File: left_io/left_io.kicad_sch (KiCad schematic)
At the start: 0 parts

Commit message: Board split Phase 2.4: trim center board, FPC boundary contracts, per-project verification
Center (ducktop2) loses the four sheets that moved to the daughterboards:
04_usb_c_io, 05_power_inputs, 06_tcp0_external_hdmi, 16_gigabit_ethernet,
and the pack-protection section of 01_power_battery (BMS board). J190 AUX
terminal moves to the left board. Center keeps 9 sheets: charger/gauge/
ship-FET (U2/U10/Q25/RS1), EC, Mu, radio, internal, radio-DB, keyboard x2,
maker, audio. 717 components.

FPC-1/2/3 boundary contracts declare the crossing nets at the center root
(30 + 35 + 4 shared nets; HUB_DS1_DP/DM are center pass-throughs).

Verification is now per-project:
- verify_design_contracts.py --project {ducktop2,left_io,right_io,bms}
  (five-port USB-C contracts split by port, HDMI/GbE run on right_io,
  pack contracts run on bms, sheet names parameterized)
- verify_schematic_closure.py --pack audits the BMS pack block
- verify_electrical_calculations.py --project bms for pack calcs
- pin review trimmed to center parts; FPC-boundary nets in ERC allowlist

Fixed while trimming: daughterboard root labels now sit on sheet-block pin
endpoints (left/right FPC nets actually connect); duplicate GND pwrflag in
power sheet; sync.parse_netlist respects the radio-daughterboard override.

Schematic gate PASS: self-check, closure audits (89+151), electrical
calcs (67+15), pin review (1625), identity.
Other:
- sheet PD1 Dual-Role ports: added none; removed HUB_DS1_DM, HUB_DS1_DP, INTERNAL_USB_VBUS_VALID, USBC2_DM, USBC2_DP, USBC2_SSRX_N, USBC2_SSRX_P, USBC2_SSTX_N, USBC2_SSTX_P, VSYS
- sheet USB Hub + Ports ports: added none; removed AUX_DC_RAW, MCU_3V3, PD1_EFUSE_FAULT_N, PD1_I2C_SCL, PD1_I2C_SDA, PD1_PATH_EN, PD1_TCPC_IRQ_N, PD1_VALID_N, PD1_VBUS_RAW, PD2_VALID_N, PD_PROTECT_FAULT_N, USBC1_DM, USBC1_DP, USBC1_SSRX_N, USBC1_SSRX_P, USBC1_SSTX_N, USBC1_SSTX_P, USB_PD_SELECTED

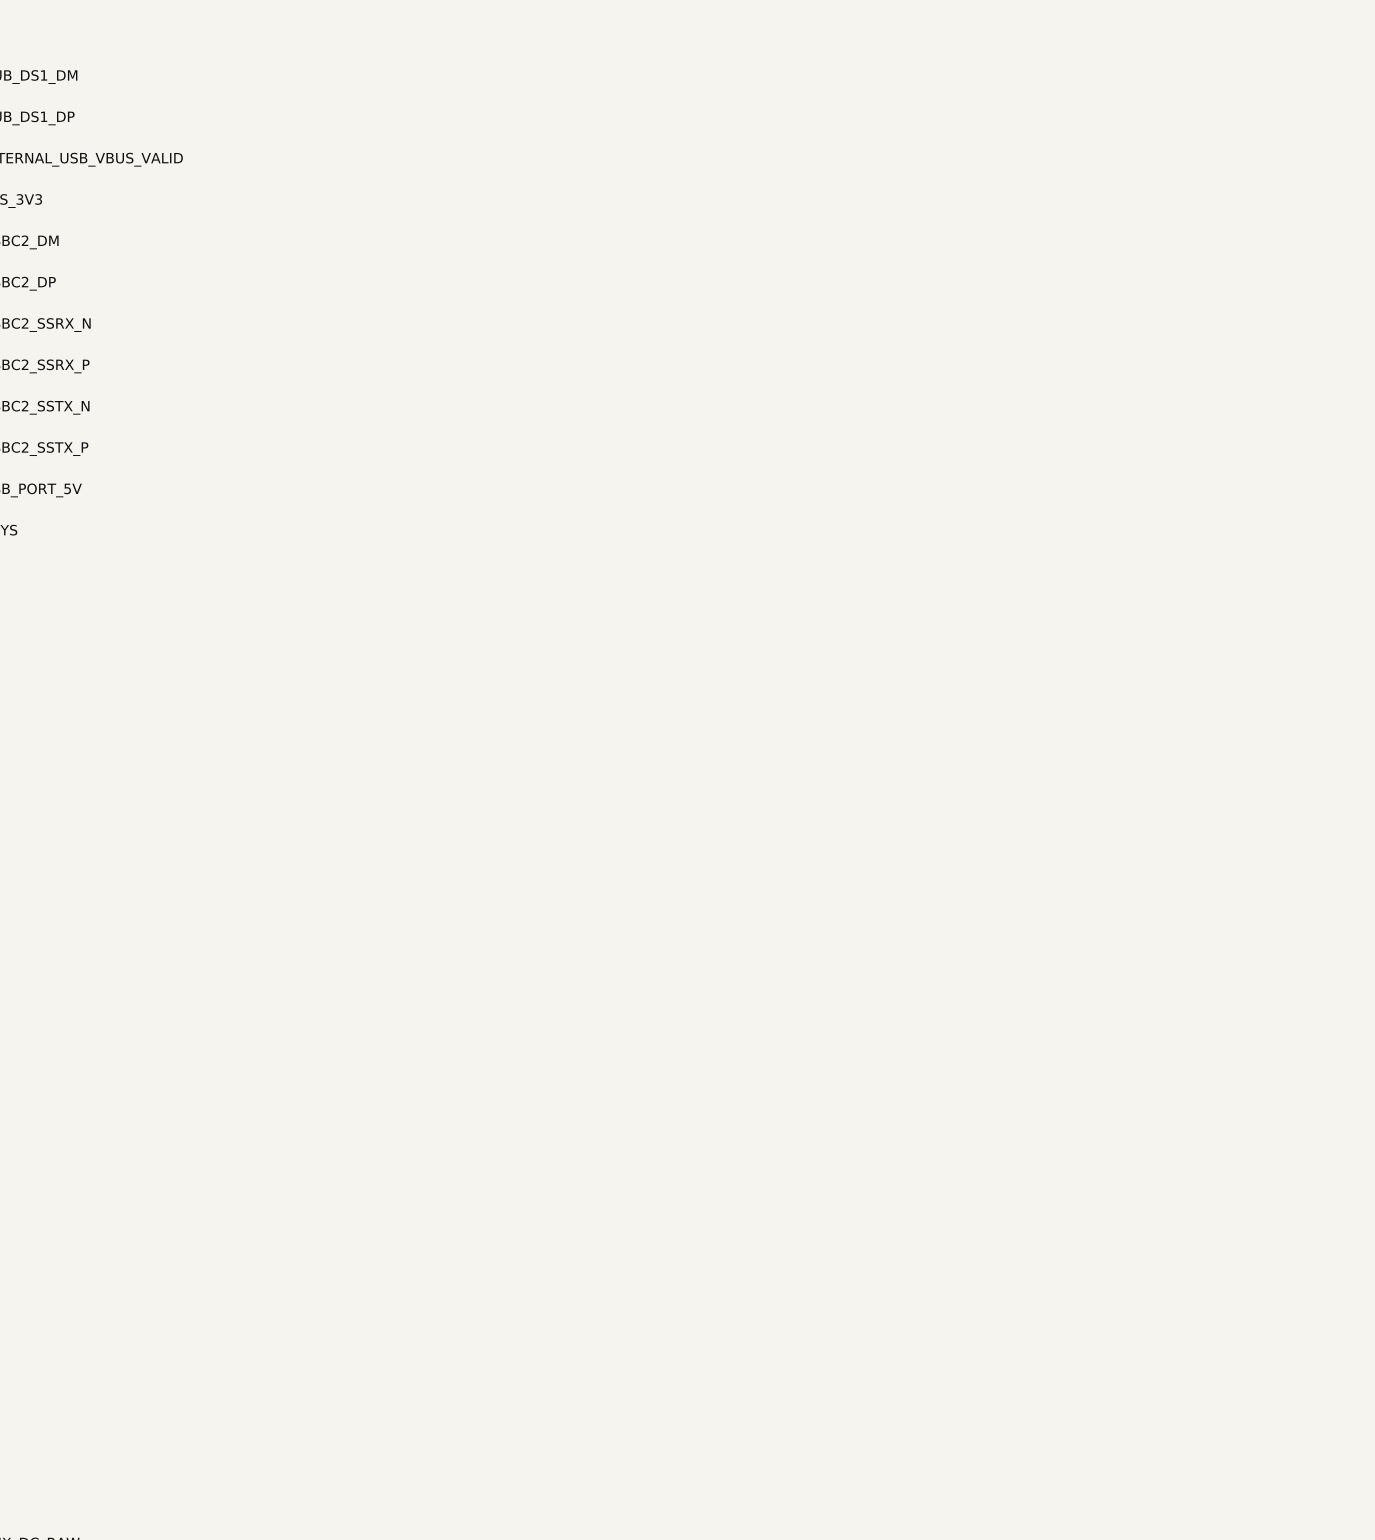
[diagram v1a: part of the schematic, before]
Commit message: Board split Phase 4a: FPC connectors wired through the four split schematics
Connector symbols and sheets now exist in every project and the boundary
nets are pinned through them (same conductor order on both ends, verified
netlist-by-netlist):
  - gen/fpc_contract.py: authoritative FPC-1/2/3 pin maps + center-side
    renames (single source of truth for schematics, board pad nets, cable
    spec, and gate contracts)
  - gen/Conn_01x100_FFC_MP.kicad_sym (derived from the 30-pin pattern)
  - center: real fpc1_left/fpc2_right/fpc3_bms sheets wired to host pins
  - left_io/right_io: left_fpc/right_fpc connector sheets; bms carries
    FPC106 inline
  - connector refs FPC101..FPC106 (valid designators; FPC1_L-style refs
    broke KiCad annotation)
  - pack-rail naming reconciled: center gauge divider BAT_PROT_VIN ->
    PACK_POS_FUSED (same node as the BMS LTC4368 output); BMS ground
    /GND -> GND (pack negative is the system ground)

Boards: daughterboards re-synced from their connector-bearing schematics;
center connectors placed and their pad nets assigned text-side ((net
"name") convention).  Connector pads verified against every other
footprint (0 overlaps) and DRC shows 0 shorts on all four boards (center
16 pre-existing, down from 17).

Fixed two latent generator bugs exposed by the wiring:
  - resolve_connectors used naive +R rotation, placing Phase 3 connectors
    against mirrored phantom positions
  - pad half-extents were computed as footprint_rot+pad_rot, but KiCad
    saves pads with world orientation (FH12-100S pins are 1.3mm wide);
    both verified empirically against pcbnew, plus a connector-nudge pass
    for parts sandwiched between the connector body and pin columns

Gate: SCHEMATIC RELEASE CHECK: PASS (FPC pin contracts added per project;
closure audits 0 FAIL).  Routing remains manual (Phase 4b).
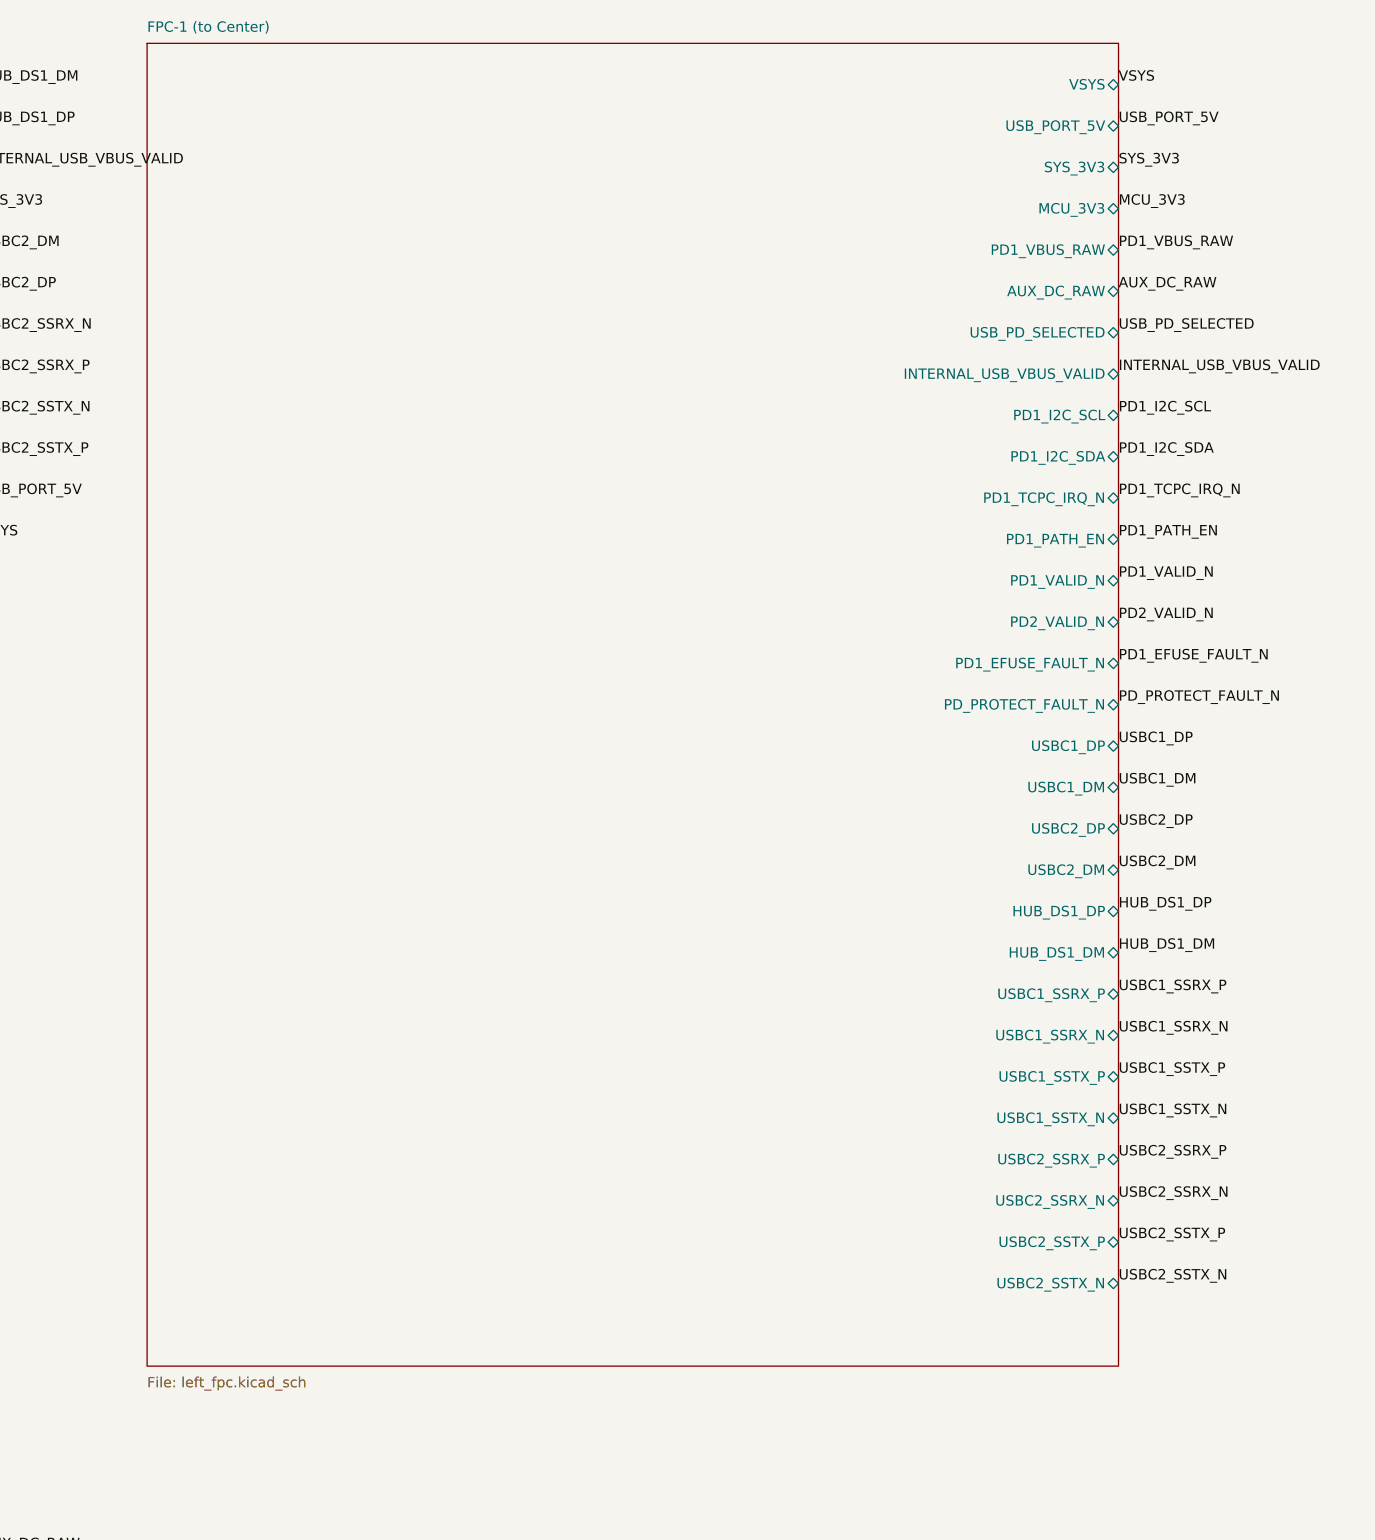
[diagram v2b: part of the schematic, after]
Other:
- added sheet FPC-1 (to Center) (left_fpc.kicad_sch)

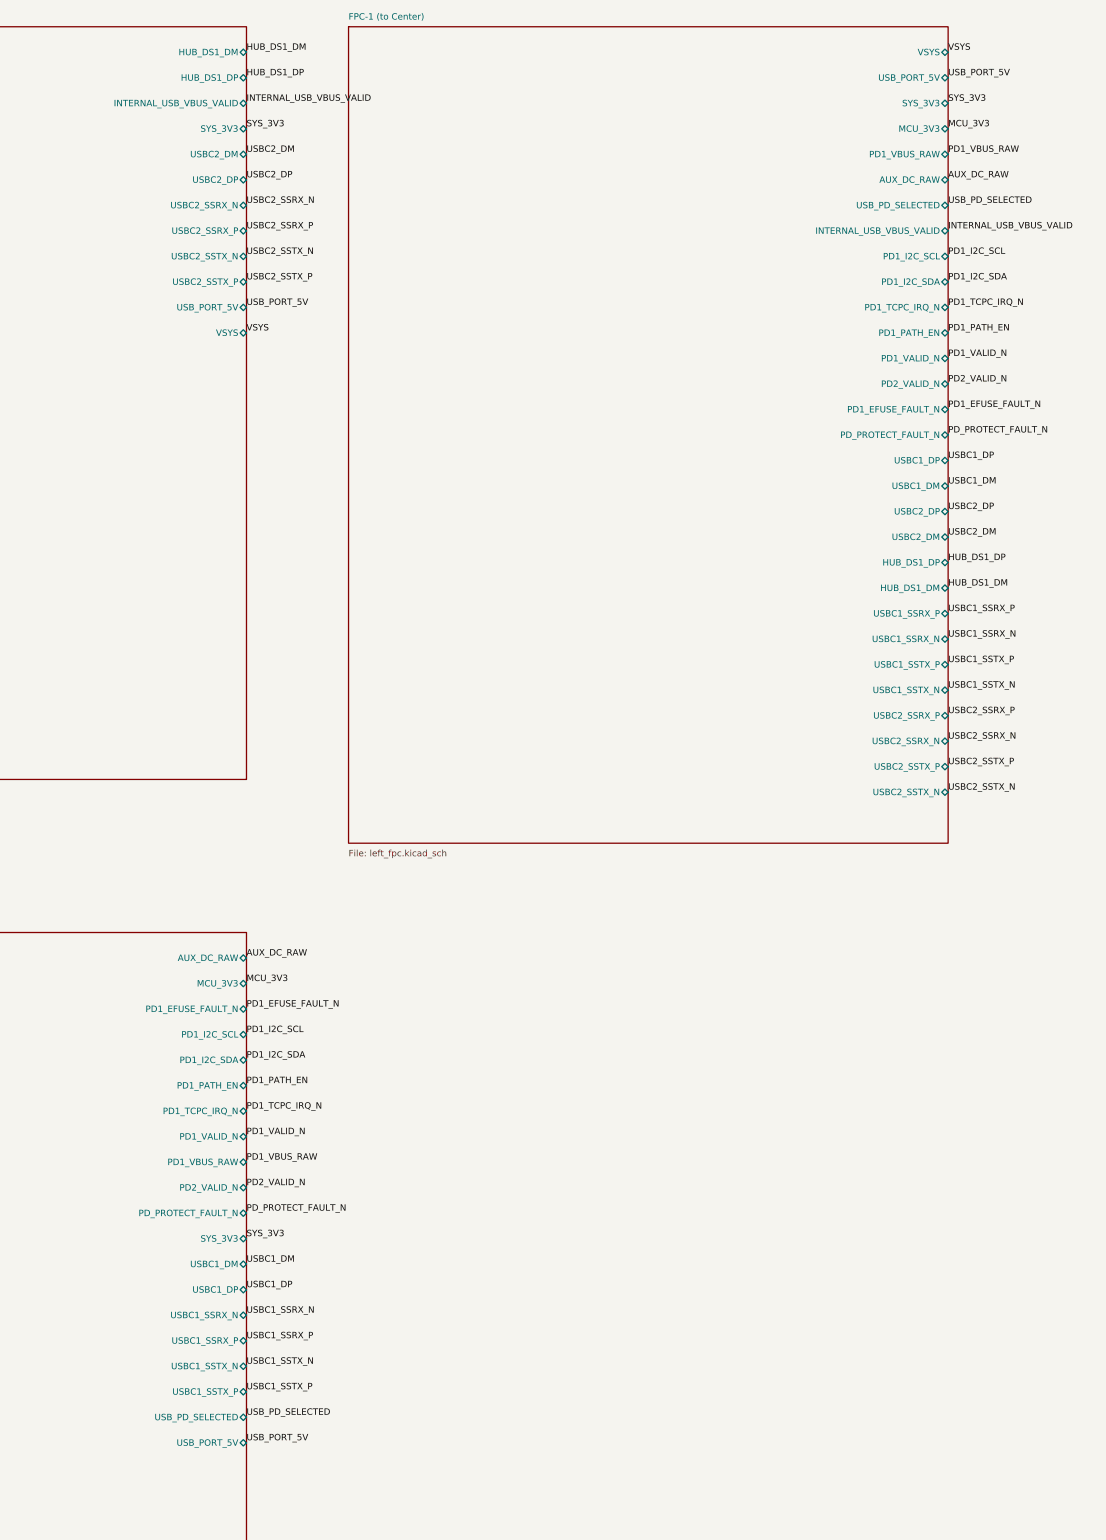
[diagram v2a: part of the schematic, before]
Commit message: Phase 5: second-opinion audit remediation + rebuilt, verified board pipeline
Second-opinion AI audit found A-tier defects; remediation applied and the
board pipeline rebuilt on a known-good base with the fixes it needed:

- electrical: LTC4418IUF symbol pinout corrected (both selectors were
  dead as drawn); center charge cascade (U15 <- U15B, PD1 > PD2 > AUX);
  pack negative never crosses FPC-3, 15-pin FG_VSS return; power-budgeted
  FPC pin maps (0.4 A/pin derate); J12/DS4 completed; AUX source fuse
- FH41-68S footprint: 13 datasheet-correct SH pads + SH pin in symbol
- connector geometry settled against the Hirose FH12 2D drawing: FFC
  enters opposite the solder pins (mouth = local +Y); reversed side-B
  maps are correct for the 180-deg-mounted pairs; rotations set so mouths
  face across every seam
- pipeline (generate_split_boards.py): per-pin pad-net resync from the
  netlists (kills shadow nets for good), netlist-exact name
  normalization, netlist-only part injection (cascade, probe headers),
  zone refill after outline swap, read-before-write race fixed, orphan
  parts dropped loudly, non-zero exit on unresolved overlaps
- monolith board relocated to old/monolith_ducktop2.kicad_pcb (placement
  oracle for the center cut only)

verified end state: 4 boards 0 shorts / 0 clearance / 0 drill, 0 boundary
crossings, 6/6 connectors contract-exact with mouths facing, 0 shadow
nets, gates PASS x4, ERC 0 x4. routing next (499 nets/board).
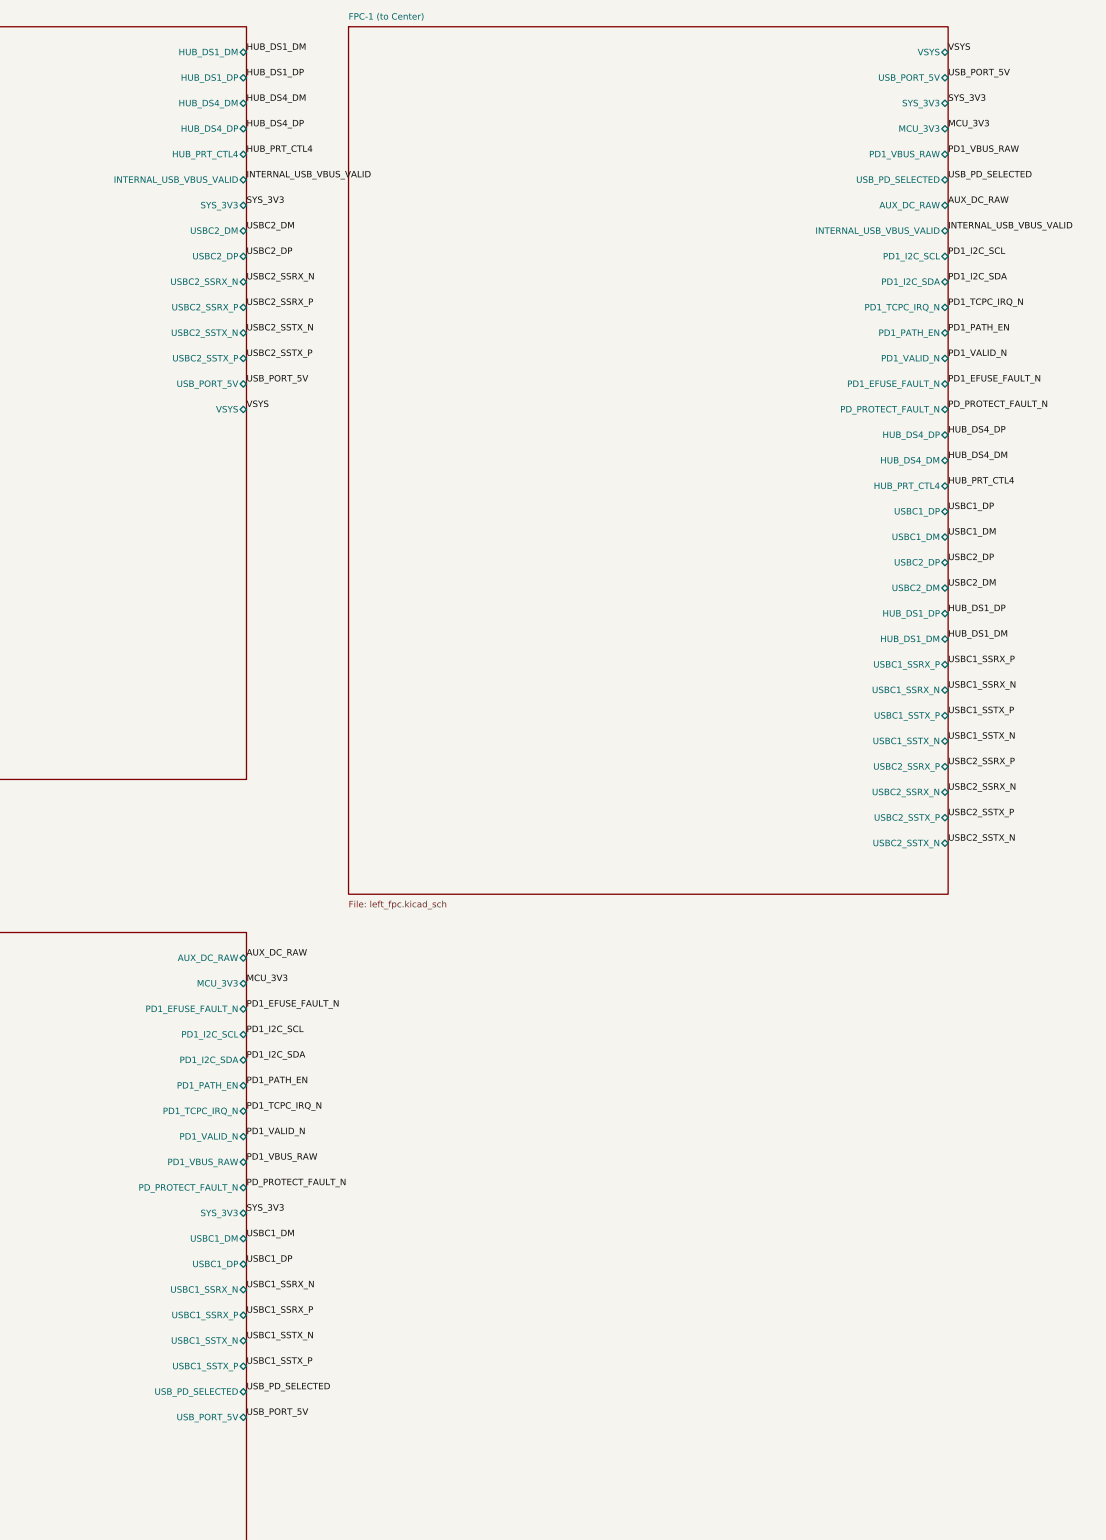
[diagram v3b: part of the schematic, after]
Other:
- sheet FPC-1 (to Center) ports: added HUB_DS4_DM, HUB_DS4_DP, HUB_PRT_CTL4; removed PD2_VALID_N
- sheet PD1 Dual-Role ports: added none; removed PD2_VALID_N
- sheet USB Hub + Ports ports: added HUB_DS4_DM, HUB_DS4_DP, HUB_PRT_CTL4; removed none
